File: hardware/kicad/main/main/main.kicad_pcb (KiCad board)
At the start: 2 copper layers, 4 parts, among them J1 USB_C_Receptacle_USB2.0, U1 CH340G, U2 ESP32-WROOM-32

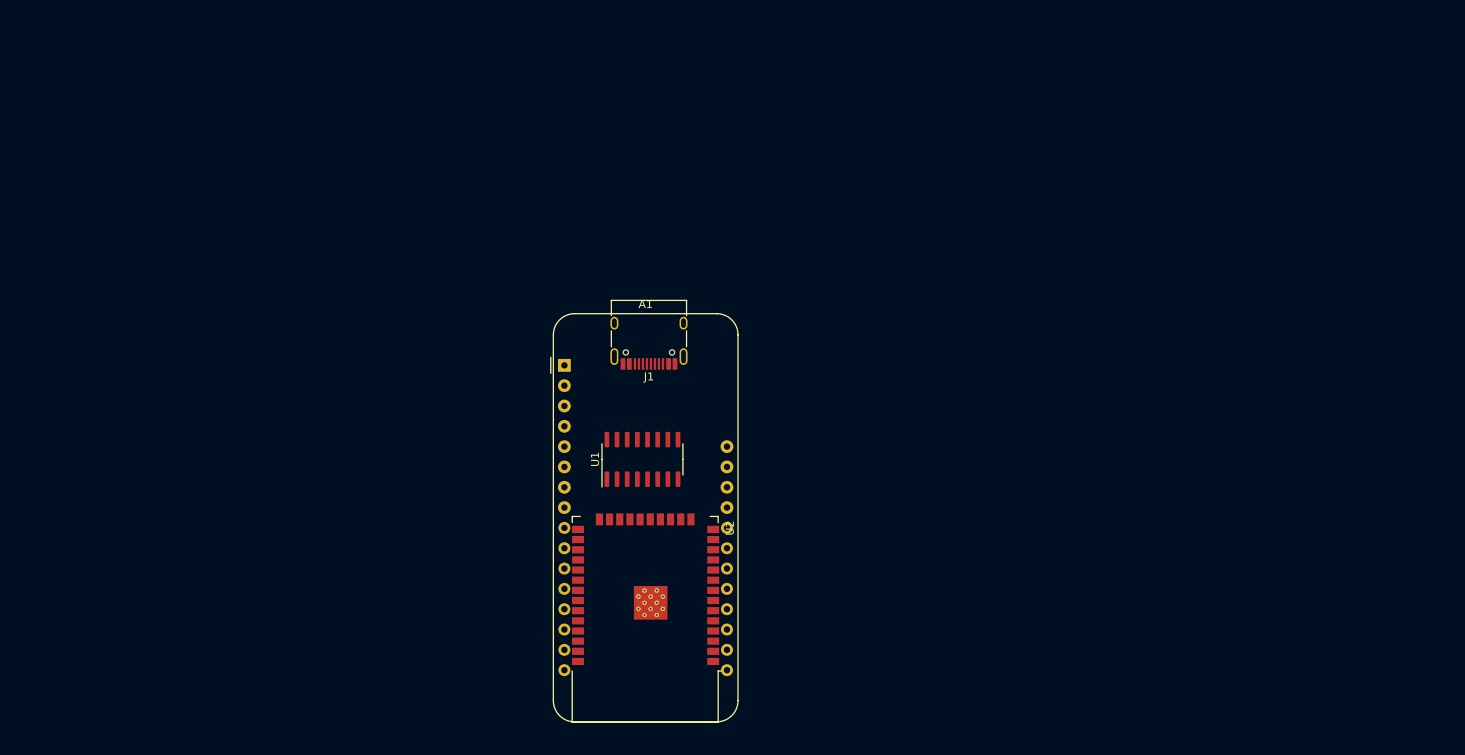
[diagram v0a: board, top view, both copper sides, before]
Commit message: added battery charging ic, mounting holes
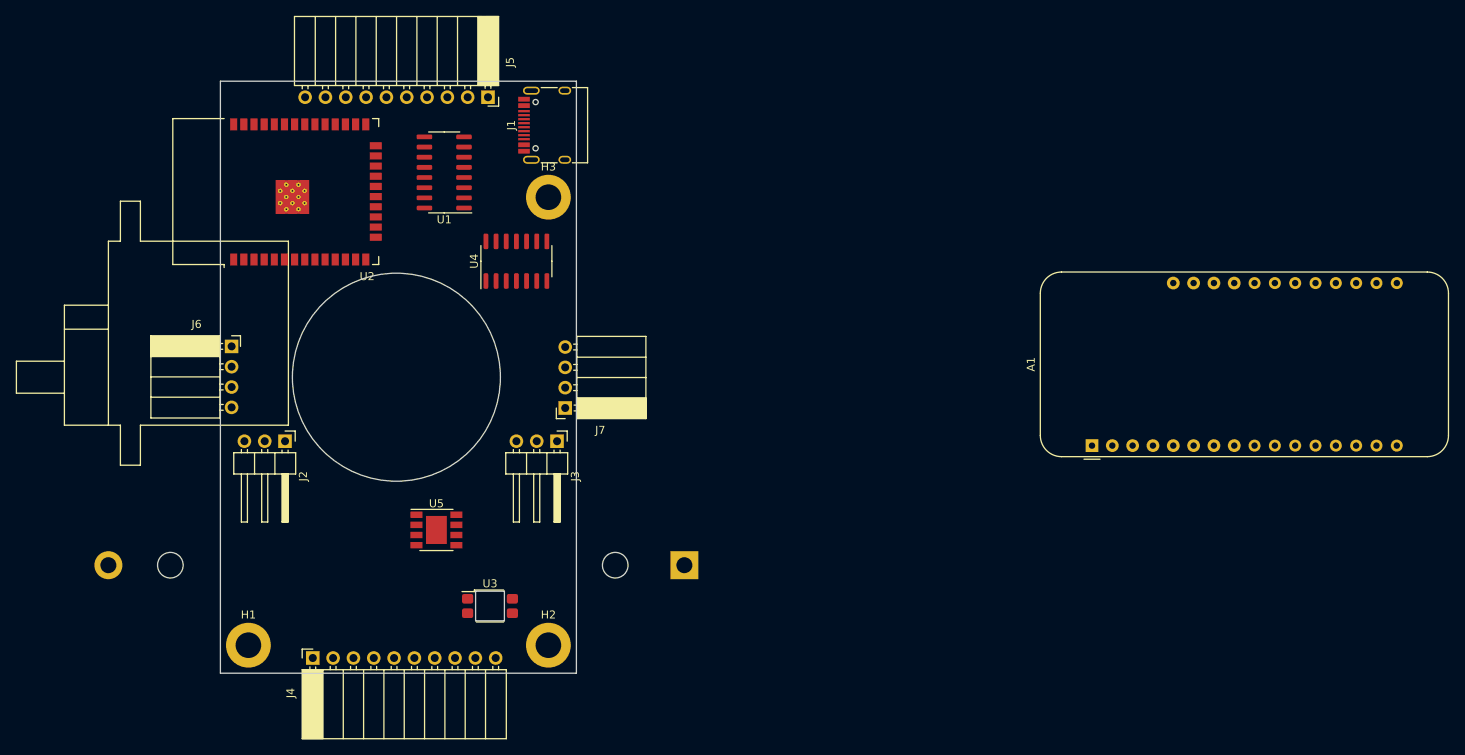
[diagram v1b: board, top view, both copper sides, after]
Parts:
- added BT1: Battery_Cell, Battery:BatteryHolder_MPD_BH-18650-PC2, B.Cu at (136.0, 123.5)
- added H1: MountingHole_Pad, MountingHole:MountingHole_3.2mm_M3_DIN965_Pad, F.Cu at (81.5, 133.5)
- added H2: MountingHole_Pad, MountingHole:MountingHole_3.2mm_M3_DIN965_Pad, F.Cu at (119.0, 133.5)
- added H3: MountingHole_Pad, MountingHole:MountingHole_3.2mm_M3_DIN965_Pad, F.Cu at (119.0, 77.5)
- added J2: SERVO_L, Connector_PinHeader_2.54mm:PinHeader_1x03_P2.54mm_Horizontal, F.Cu at (86.1, 108.0)
- added J3: SERVO_R, Connector_PinHeader_2.54mm:PinHeader_1x03_P2.54mm_Horizontal, F.Cu at (120.1, 108.0)
- added J4: EXP_FRONT, Connector_PinSocket_2.54mm:PinSocket_1x10_P2.54mm_Horizontal, F.Cu at (89.5, 135.1)
- added J5: EXP_BACK, Connector_PinSocket_2.54mm:PinSocket_1x10_P2.54mm_Horizontal, F.Cu at (111.5, 65.0)
- added J6: ENC_LEFT, Connector_PinSocket_2.54mm:PinSocket_1x04_P2.54mm_Horizontal, F.Cu at (79.4, 96.2)
- added J7: ENC_RIGHT, Connector_PinSocket_2.54mm:PinSocket_1x04_P2.54mm_Horizontal, F.Cu at (121.1, 103.8)
- added REF**: mg90s, mg90s, B.Cu at (132.0, 100.0)
- added REF**: mg90s_right, mg90s:mg90s_right, B.Cu at (68.0, 100.0)
- added U3: ITR8307, OptoDevice:Everlight_ITR8307, F.Cu at (111.7, 128.6)
- added U4: LM339, Package_SO:SOIC-14_3.9x8.7mm_P1.27mm, F.Cu at (115.0, 85.5)
- added U5: IP5306, Package_SO:Diodes_SO-8EP, F.Cu at (105.0, 119.1)
- moved A1 66.7 mm to (186.9, 108.6), turned to 90 degrees
- moved U2 66.4 mm to (87.9, 76.8), turned to 90 degrees
- moved U1 43.6 mm to (106.0, 74.4), turned to 180 degrees
- moved J1 28.3 mm to (120.0, 68.5), turned to 90 degrees
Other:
- board outline added: 44.5 x 74 mm
